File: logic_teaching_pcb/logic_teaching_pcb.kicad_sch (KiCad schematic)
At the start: 88 parts, among them J1 Conn_01x02, J13 Conn_01x02, J14 Conn_01x01, J15 Conn_01x02, J16 Conn_01x01, J17 Conn_01x01, J18 Conn_01x01, J2 Conn_01x02, J25 Conn_01x02, J26 Conn_01x01, J27 Conn_01x02, J28 Conn_01x01, J29 Conn_01x02, J3 Conn_01x02, J30 Conn_01x02, J31 Conn_01x02, J32 Conn_01x01, J33 Conn_01x02, J34 Conn_01x01, J35 Conn_01x02, J36 Conn_01x01, J37 Conn_01x02, J38 Conn_01x01, J39 Conn_01x02, J4 Conn_01x02, J40 Conn_01x01, J41 Conn_01x02, J42 Conn_01x01, J43 Conn_01x02, J44 Conn_01x01, J45 Conn_01x01, J46 Conn_01x02, J47 Conn_01x01, J48 Conn_01x02, J49 Conn_01x01, J5 Conn_01x01, J50 Conn_01x02, J51 Conn_01x01, J52 Conn_01x02, J53 Conn_01x01, J54 Conn_01x02, J55 Conn_01x01, J56 Conn_01x01, J57 Conn_01x01, J58 Conn_01x01, J59 Conn_01x02, J6 Conn_01x01, J60 Conn_01x02, J61 Conn_01x02, J62 Conn_01x02, J63 Conn_01x01, J64 Conn_01x01, J65 Conn_01x01, J66 Conn_01x01, J7 Conn_01x01, J8 Conn_01x01, J9 Conn_01x01, SW1 SW_SPDT, SW5 SW_Push, SW6 SW_Push, SW7 SW_Push, SW8 SW_Push, U1 74HC00, U2 74HC00

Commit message: finish first PCB draft
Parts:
- added J10, J12: Conn_01x02, Connector_PinHeader_2.54mm:PinHeader_1x02_P2.54mm_Vertical, symbol Connector_Generic:Conn_01x02
- added J11, J70: Conn_01x01, Connector:Banana_Jack_1Pin, symbol Connector_Generic:Conn_01x01
- added J19, J20, J21, J22, J23, J24, J67, J68, J69: Conn_01x01, Connector_PinHeader_2.54mm:PinHeader_1x01_P2.54mm_Vertical, symbol Connector_Generic:Conn_01x01
- added SW2, SW3, SW4: SW_SPDT, Button_Switch_THT:SW_Slide_1P2T_CK_OS102011MS2Q, symbol Switch:SW_SPDT
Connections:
- net GND: now also J12.1 (Pin_1), J12.2 (Pin_2), J70.1 (Pin_1)
- net +3V0: no longer names the net of R1.2
- net +3V0: now also J10.1 (Pin_1), J10.2 (Pin_2), J11.1 (Pin_1)
- new net: J19.1 (Pin_1), SW2.2 (B)
- new net: J21.1 (Pin_1), SW2.3 (C)
- new net: J22.1 (Pin_1), SW3.2 (B)
- new net: J69.1 (Pin_1), SW4.3 (C)
- new net: J67.1 (Pin_1), SW4.2 (B)
- new net: J20.1 (Pin_1), SW2.1 (A)
- new net: J24.1 (Pin_1), SW3.3 (C)
- new net: J68.1 (Pin_1), SW4.1 (A)
- new net: J23.1 (Pin_1), SW3.1 (A)
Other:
- note added: "Banana or 0.1" external power"
- note added: "GND connectors for user"
- note added: "Protection resistor: min. 1W rated power dissipation"
- note added: "V+ connectors for user"
- note removed: "min. 1W rated power dissipation"
- moved on the sheet: BT1, J30, J31, R1

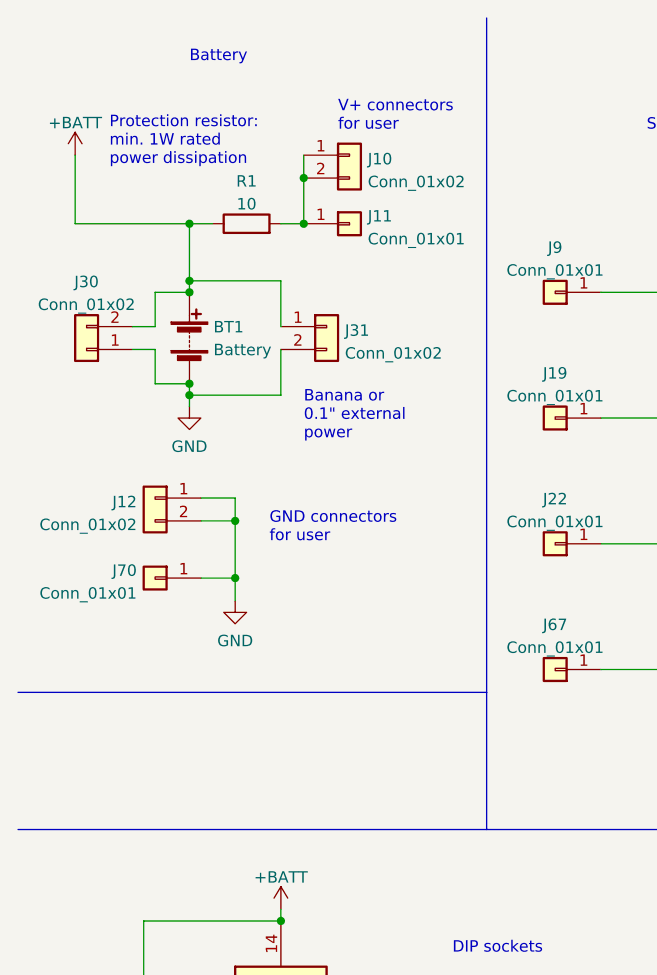
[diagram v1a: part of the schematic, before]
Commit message: Added power switch
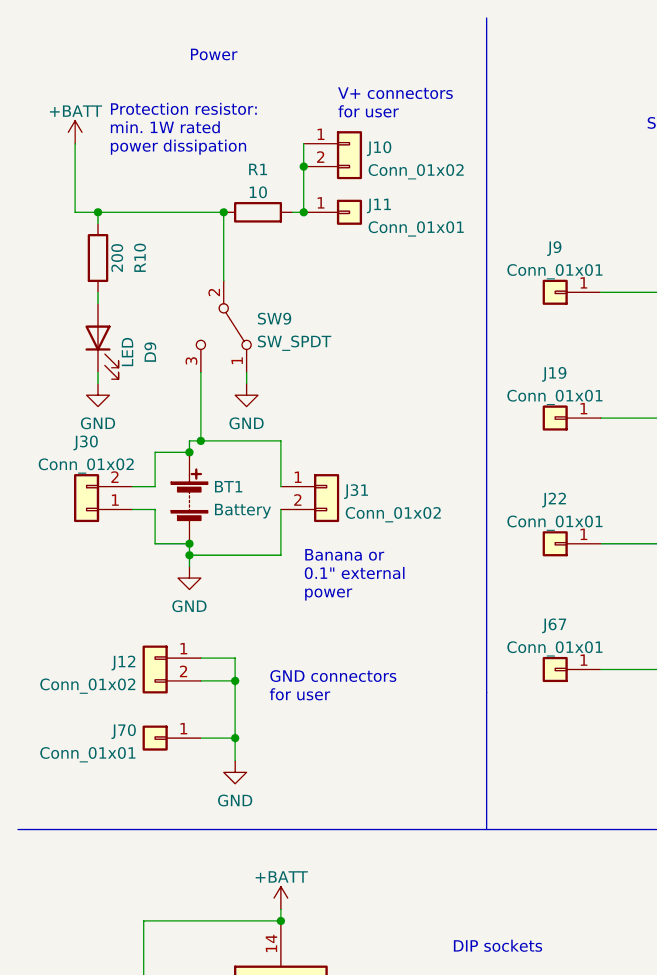
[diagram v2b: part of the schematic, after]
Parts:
- added D9: LED, LED_SMD:LED_1206_3216Metric_Pad1.42x1.75mm_HandSolder, symbol Device:LED
- added R10: 200, Resistor_SMD:R_1206_3216Metric_Pad1.30x1.75mm_HandSolder, symbol Device:R
- added SW9: SW_SPDT, Button_Switch_THT:SW_Slide_1P2T_CK_OS102011MS2Q, symbol Switch:SW_SPDT
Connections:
- net +BATT: now also R10.1, SW9.2 (B); no longer BT1.1 (+), J30.2 (Pin_2), J31.1 (Pin_1)
- net GND: now also D9.1 (K), SW9.1 (A)
- new net: BT1.1 (+), J30.2 (Pin_2), J31.1 (Pin_1), SW9.3 (C)
- new net: D9.2 (A), R10.2
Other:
- note added: "Power"
- note removed: "Battery"
- moved on the sheet: BT1, J10, J11, J12, J30, J31, J70, R1

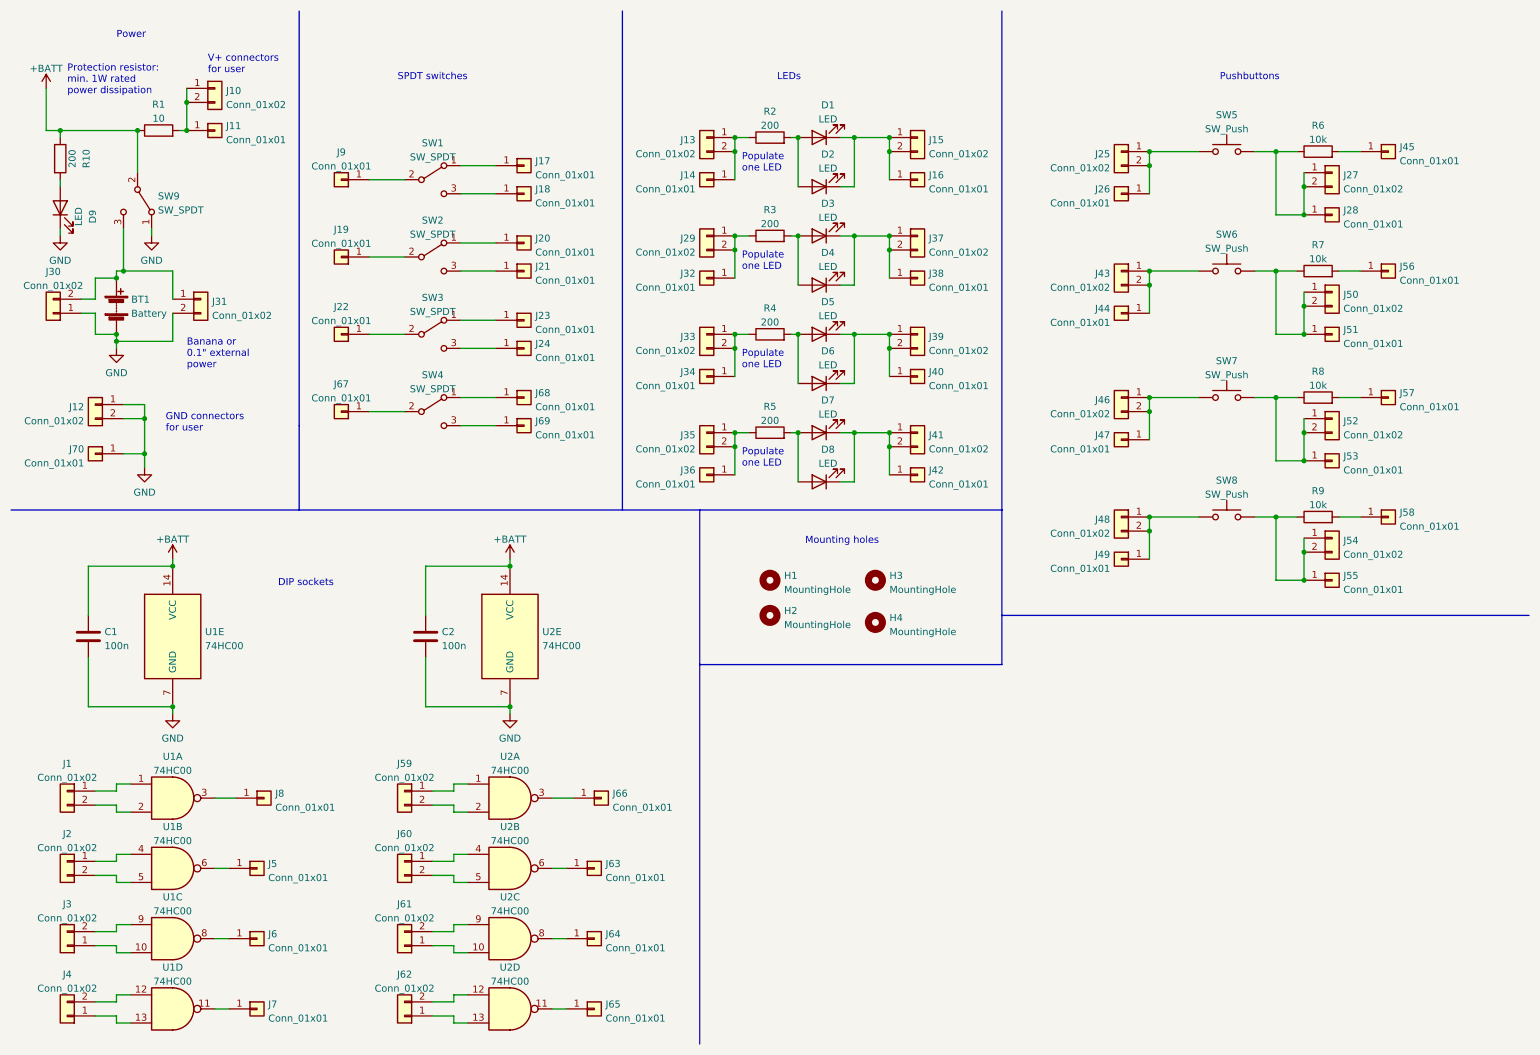
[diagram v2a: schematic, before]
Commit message: change footprint to binding post, add to switches
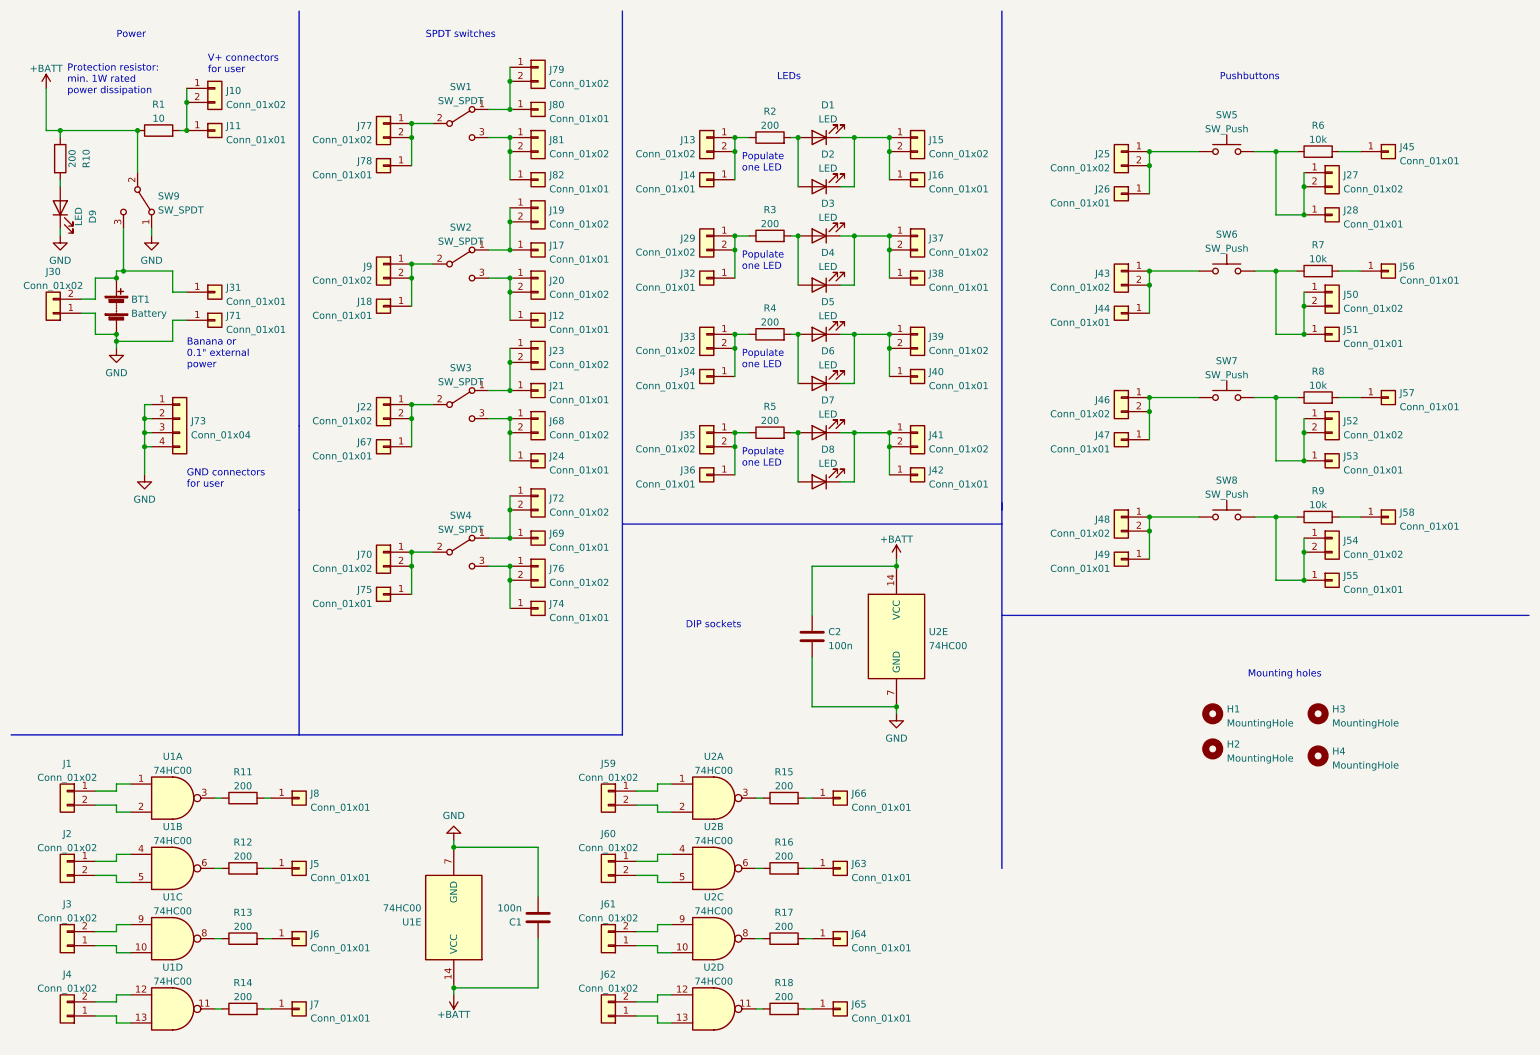
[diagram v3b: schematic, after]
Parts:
- removed J12: Conn_01x02, Connector_PinHeader_2.54mm:PinHeader_1x02_P2.54mm_Vertical, symbol Connector_Generic:Conn_01x02
- removed J19, J20, J22, J23, J68, J9: Conn_01x01, Connector_PinHeader_2.54mm:PinHeader_1x01_P2.54mm_Vertical, symbol Connector_Generic:Conn_01x01
- removed J31: Conn_01x02, Connector:Banana_Jack_2Pin, symbol Connector_Generic:Conn_01x02
- removed J70: Conn_01x01, Connector:Banana_Jack_1Pin, symbol Connector_Generic:Conn_01x01
- added J12, J31, J71, J74, J75, J78, J80, J82: Conn_01x01, Library:BindingPost_Shin_Chin_R1-9, symbol Connector_Generic:Conn_01x01
- added J19, J20, J22, J23, J68, J70, J72, J76, J77, J79, J81, J9: Conn_01x02, Connector_PinHeader_2.54mm:PinHeader_1x02_P2.54mm_Vertical, symbol Connector_Generic:Conn_01x02
- added J73: Conn_01x04, Connector_PinHeader_2.54mm:PinHeader_2x02_P2.54mm_Vertical, symbol Connector_Generic:Conn_01x04
- added R11, R12, R13, R14, R15, R16, R17, R18: 200, Resistor_SMD:R_1206_3216Metric_Pad1.30x1.75mm_HandSolder, symbol Device:R
- J11, J14, J16, J26, J28, J32, J34, J36, J38, J40, J42, J44, J47, J49, J51, J53, J55: footprint Connector:Banana_Jack_1Pin -> Library:BindingPost_Shin_Chin_R1-9
- J17, J18, J21, J24, J67, J69: footprint Connector_PinHeader_2.54mm:PinHeader_1x01_P2.54mm_Vertical -> Library:BindingPost_Shin_Chin_R1-9
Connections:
- net GND: now also J71.1 (Pin_1), J73.1 (Pin_1), J73.2 (Pin_2), J73.3 (Pin_3), J73.4 (Pin_4)
- net at BT1.1 (+), J30.2 (Pin_2), SW9.3 (C): now also J31.1 (Pin_1)
- net at SW2.2 (B): now also J18.1 (Pin_1), J9.1 (Pin_1), J9.2 (Pin_2)
- net at J17.1 (Pin_1): now also SW2.1 (A), J19.1 (Pin_1), J19.2 (Pin_2); no longer SW1.1 (A)
- net at SW1.2 (B): now also J77.1 (Pin_1), J77.2 (Pin_2), J78.1 (Pin_1)
- net at SW1.3 (C): now also J81.1 (Pin_1), J81.2 (Pin_2), J82.1 (Pin_1); no longer J18.1 (Pin_1)
- net at SW2.3 (C): now also J12.1 (Pin_1), J20.1 (Pin_1), J20.2 (Pin_2); no longer J21.1 (Pin_1)
- net at J63.1 (Pin_1): now also R16.2; no longer U2.6
- net at SW3.2 (B): now also J67.1 (Pin_1), J22.1 (Pin_1), J22.2 (Pin_2)
- net at U1.8: now also R13.1; no longer J6.1 (Pin_1)
- net at SW4.3 (C): now also J74.1 (Pin_1), J76.1 (Pin_1), J76.2 (Pin_2); no longer J69.1 (Pin_1)
- net at U1.3: now also R11.1; no longer J8.1 (Pin_1)
- net at J66.1 (Pin_1): now also R15.2; no longer U2.3
- net at SW4.2 (B): now also J70.1 (Pin_1), J70.2 (Pin_2), J75.1 (Pin_1); no longer J67.1 (Pin_1)
- net at J24.1 (Pin_1), SW3.3 (C): now also J68.1 (Pin_1), J68.2 (Pin_2)
- net at J5.1 (Pin_1): now also R12.2; no longer U1.6
- net at SW4.1 (A): now also J69.1 (Pin_1), J72.1 (Pin_1), J72.2 (Pin_2)
- net at J7.1 (Pin_1): now also R14.2; no longer U1.11
- net at SW3.1 (A): now also J21.1 (Pin_1), J23.1 (Pin_1), J23.2 (Pin_2)
- net at U2.8: now also R17.1; no longer J64.1 (Pin_1)
- net at U2.11: now also R18.1; no longer J65.1 (Pin_1)
- new net: J79.1 (Pin_1), J79.2 (Pin_2), J80.1 (Pin_1), SW1.1 (A)
- new net: J64.1 (Pin_1), R17.2
- new net: R16.1, U2.6
- new net: R12.1, U1.6
- new net: J65.1 (Pin_1), R18.2
- new net: J8.1 (Pin_1), R11.2
- new net: R14.1, U1.11
- new net: R15.1, U2.3
- new net: J6.1 (Pin_1), R13.2
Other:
- moved on the sheet: C1, C2, H1, H2, H3, H4, J5, J59, J6, J60, J61, J62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
